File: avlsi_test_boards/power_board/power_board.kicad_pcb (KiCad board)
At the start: 4 copper layers, 100 x 100 mm, 100 parts, among them J1 PJ-102AH, J2 PJ-102AH, U1 TLV1117LV18DCYR, U11 TLV75709PDBV, U12 SN74LVC16T245DLR, U13 SN74LVC16T245DLR, U14 SN74LVC16T245DLR, U15 SN74LVC16T245DLR, U16 SN74LVC16T245DLR, U17 SN74LVC16T245DLR, U2 TLV1117LV25DCYR, U3 TLV1117LV33DCYR, U4 DS04-254-2-04BK-SMT, U5 74HC4051D_653, U6 TLV1117LV18DCYR, U7 TLV75709PDBV, U8 TLV1117LV25DCYR, U9 TLV1117LV33DCYR

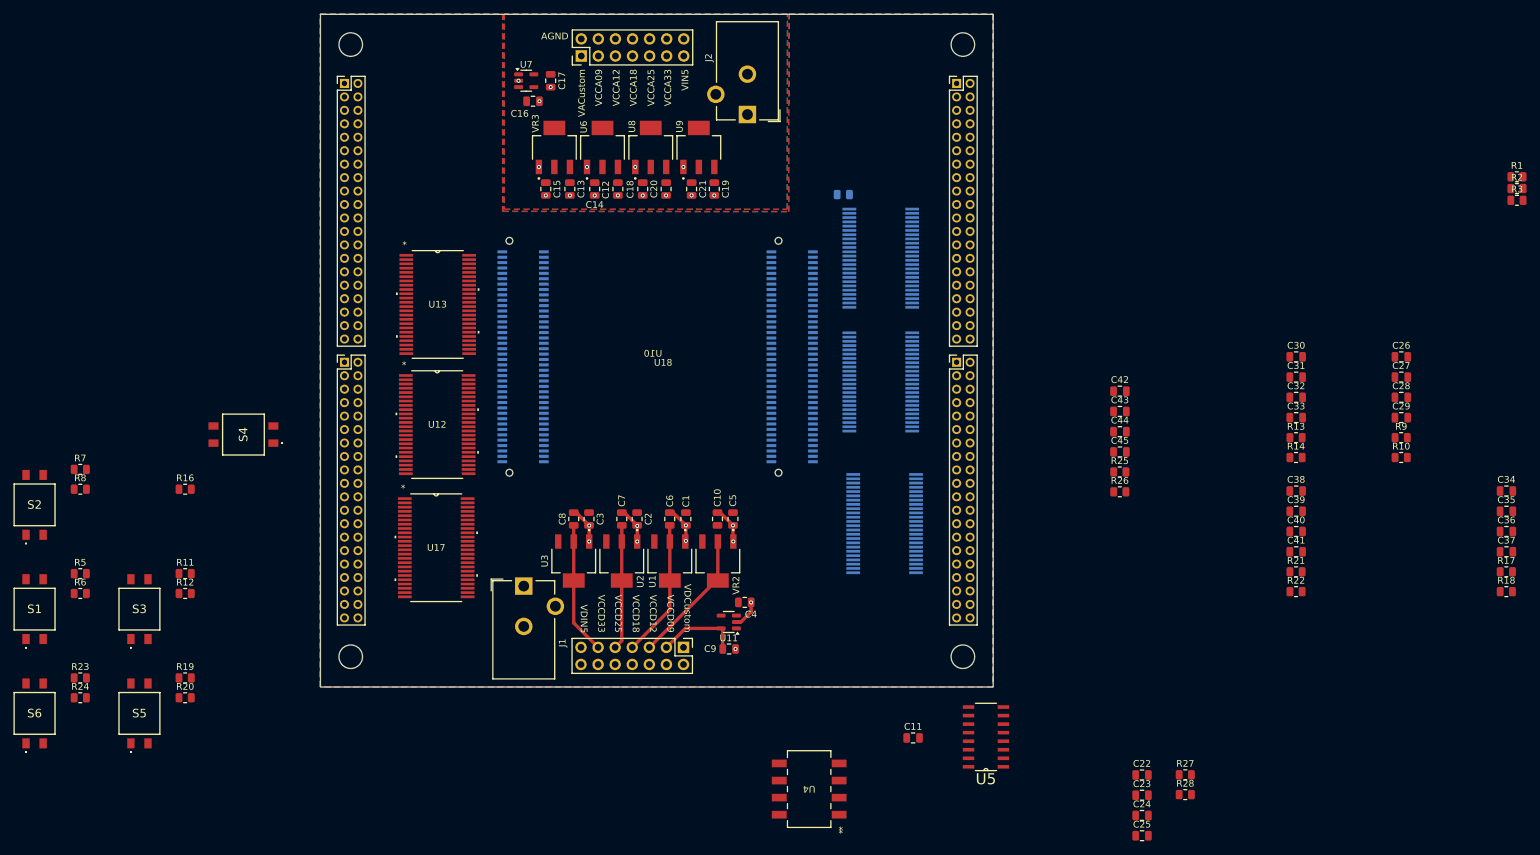
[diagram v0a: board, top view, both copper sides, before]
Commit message: Add 6 layer version of board
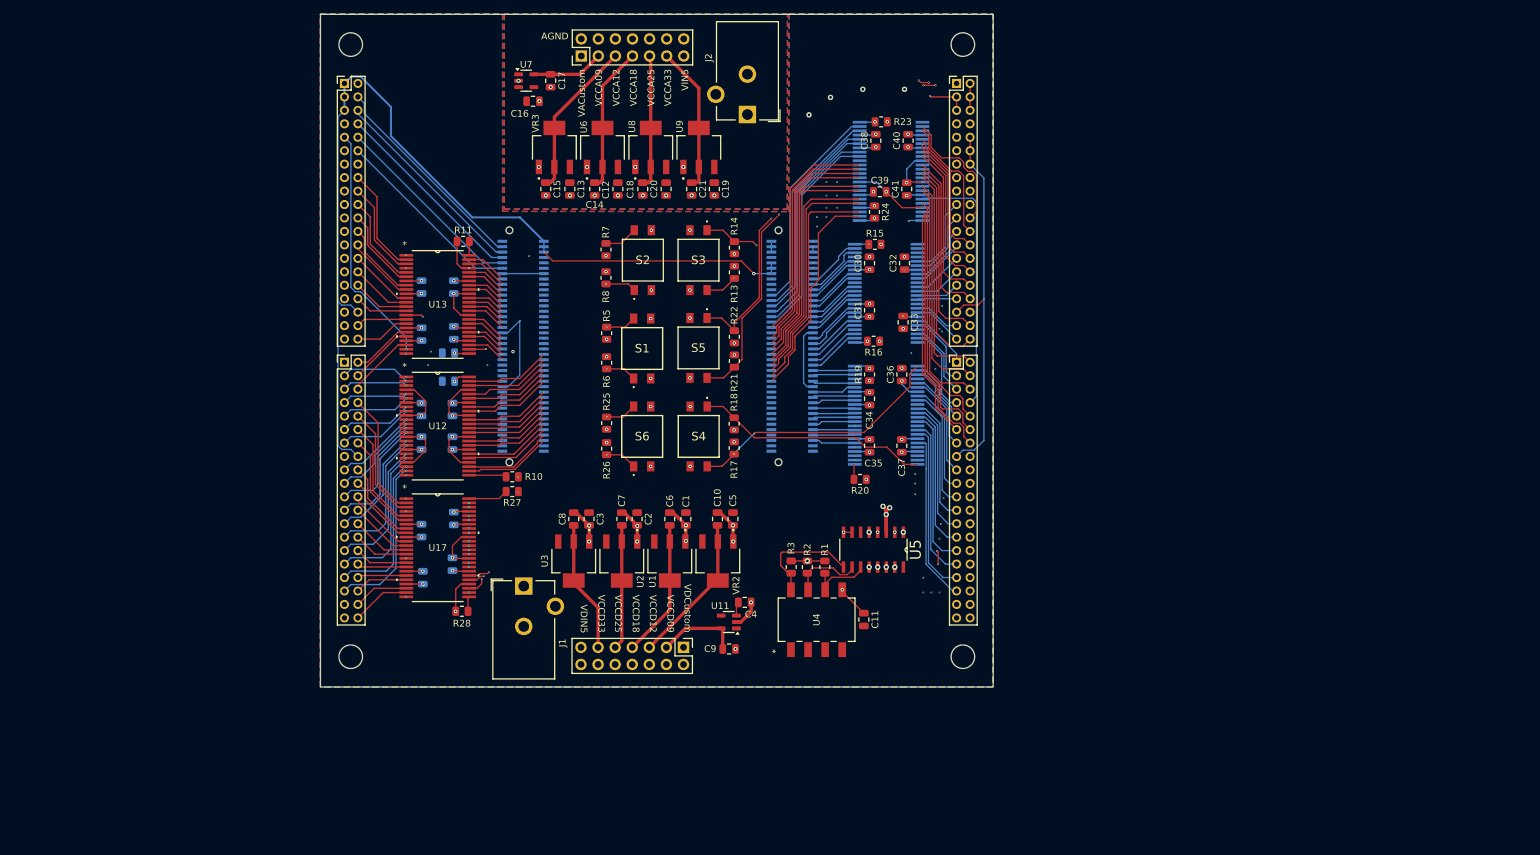
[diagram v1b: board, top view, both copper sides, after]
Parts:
- C22, C23, C24, C25, C26, C27, C28, C29, C42, C43, C44, C45, R12, R9: moved to B.Cu
- R15: moved to F.Cu
- moved C29 145.7 mm to (115.2, 89.2), turned to 90 degrees
- moved C28 145.7 mm to (115.2, 84.2), turned to -90 degrees
- moved R23 144.9 mm to (183.5, 41.4), turned to 180 degrees
- moved R9 141.9 mm to (119.2, 80.0)
- moved C27 141.4 mm to (119.8, 89.2), turned to 90 degrees
- moved C26 141.3 mm to (119.8, 84.2), turned to -90 degrees
- moved R24 138.4 mm to (182.5, 54.8), turned to -90 degrees
- moved C25 134.6 mm to (115.2, 66.0), turned to -90 degrees
- moved R10 132.2 mm to (128.7, 94.2), turned to 180 degrees
- moved C24 128.8 mm to (115.2, 73.0), turned to -90 degrees
- moved C22 125.4 mm to (120.0, 66.0), turned to -90 degrees
- moved C23 123.3 mm to (120.0, 72.8), turned to -90 degrees
- moved R3 120.9 mm to (170.2, 107.6), turned to -90 degrees
- moved R2 119.6 mm to (172.6, 107.6), turned to -90 degrees
- moved R1 118.1 mm to (175.2, 107.6), turned to -90 degrees
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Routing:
- net FPGA_33VDD: track 0.00 -> 272.7 mm, vias 0 -> 7
- net DGND: track 26.3 -> 155.3 mm, vias 10 -> 121
- net VCCD33: track 19.6 -> 100.2 mm, vias 0 -> 25
- net XADC_VP: track 0.00 -> 60.0 mm, vias 0 -> 1
- net FPGA_18VDD: track 0.00 -> 57.8 mm, vias 0 -> 1
- net XADC_VN: track 0.00 -> 57.6 mm, vias 0 -> 3
- net FPGA_VCDIN: track 0.00 -> 57.4 mm, vias 0 -> 1
- net /level_shifter5/DIR1: track 0.00 -> 57.1 mm, vias 0 -> 2
- net SYS_CLK_MC1: track 0.00 -> 54.2 mm, vias 0 -> 3
- net /level_shifter1/DIR2: track 0.00 -> 47.4 mm, vias 0 -> 2
- net /level_shifter5/DIR2: track 0.00 -> 47.1 mm, vias 0 -> 2
- net FPGA_TDO: track 0.00 -> 46.7 mm, vias 0 -> 1
- net MC1_79: track 0.00 -> 45.8 mm, vias 0 -> 1
- net VCCD18: track 20.5 -> 66.3 mm, vias 0 -> 1
- net MC1_77: track 0.00 -> 45.4 mm, vias 0 -> 1
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- added copper zone on In3.Cu, net DGND
- added copper zone on In4.Cu, net DGND
- added copper zone on In1.Cu, net VCCD33
- added copper zone on In2.Cu, net V_Level_Shift
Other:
- copper layers 4 -> 6

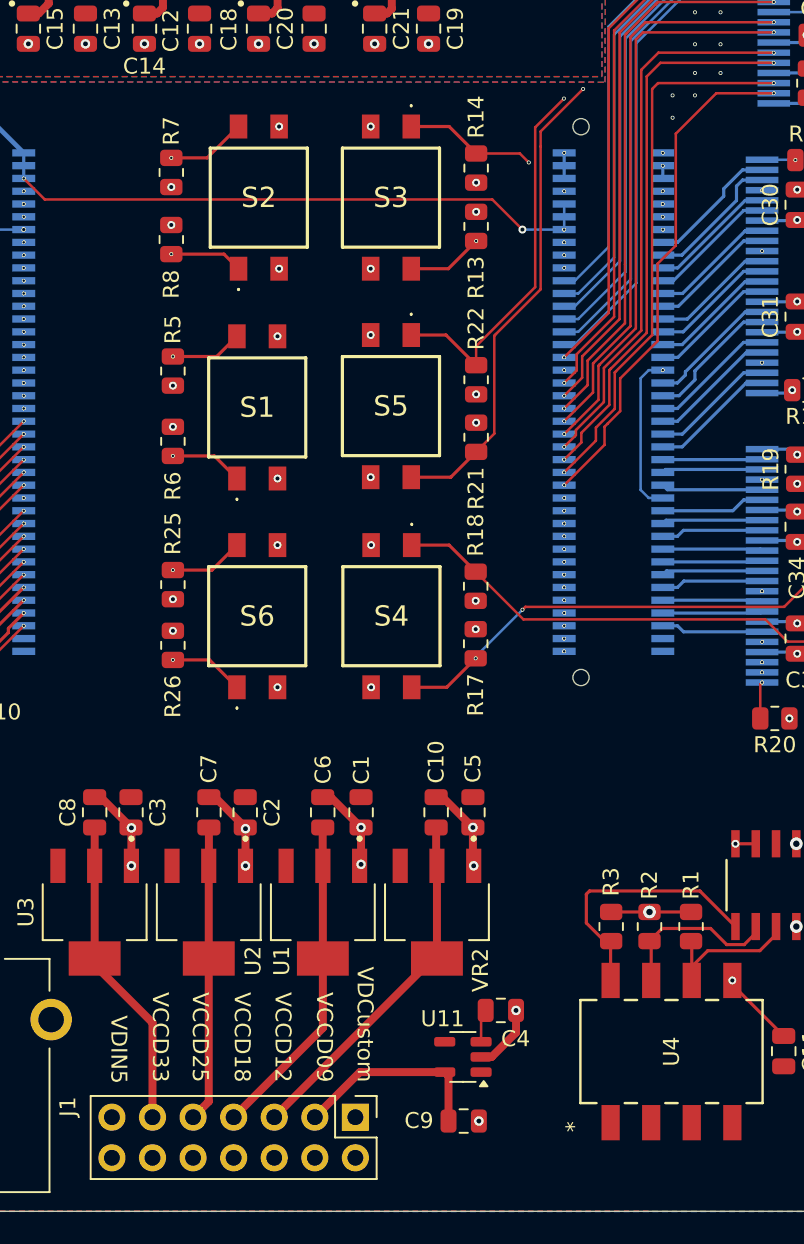
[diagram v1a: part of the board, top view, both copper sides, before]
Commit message: Add labels
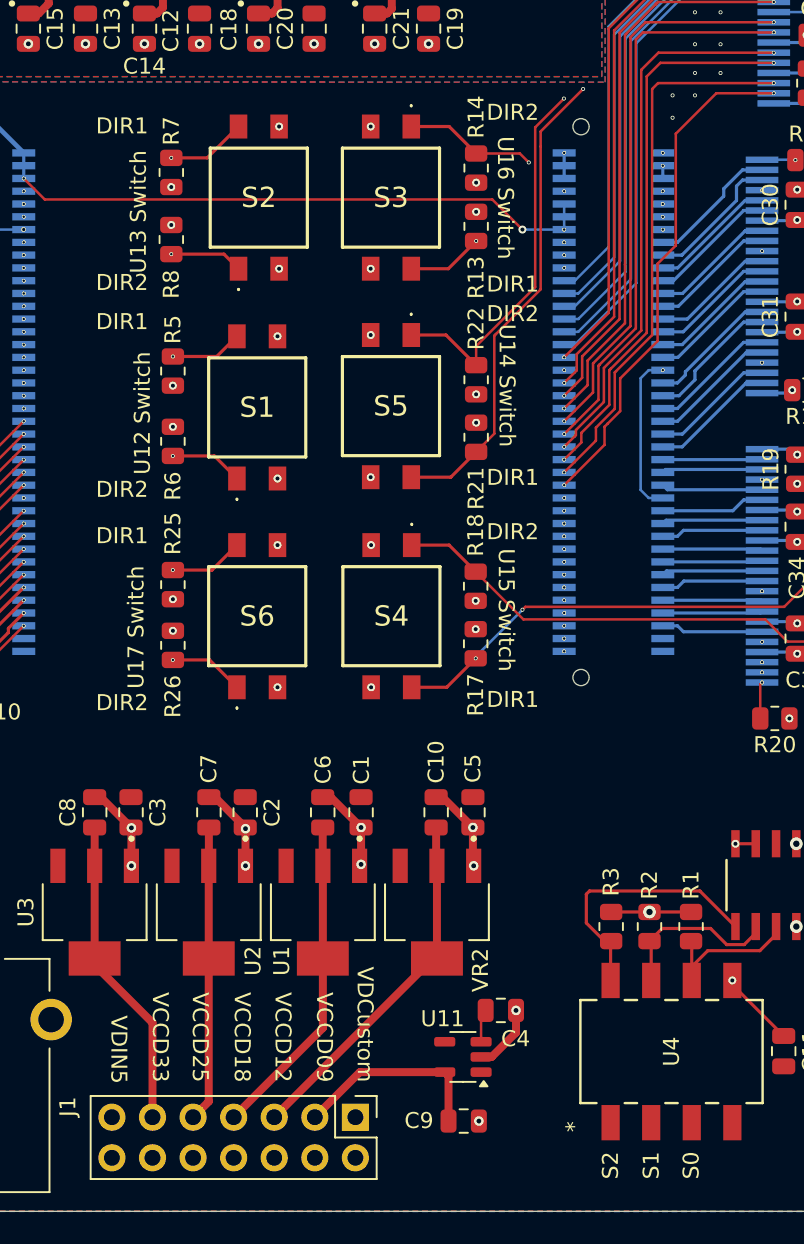
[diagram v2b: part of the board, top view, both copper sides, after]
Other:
- board text added: "DIR1"
- board text added: "DIR2"
- board text added: "S0"
- board text added: "S1"
- board text added: "S2"
- board text added: "U12 Switch"
- board text added: "U13 Switch"
- board text added: "U14 Switch"
- board text added: "U15 Switch"
- board text added: "U16 Switch"
- board text added: "U17 Switch"
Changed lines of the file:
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@@
+		)
+	)
+	(gr_text "DIR1"
+		(at 137.9 70.35 0)
+		(layer "F.SilkS")
+		(effects
+			(font
+				(size 1 1)
+				(thickness 0.15)
+			)
+			(justify left bottom)
 		)
 	)
@@
 		)
 	)
+	(gr_text "DIR1"
+		(at 137.9 83.75 0)
+		(layer "F.SilkS")
+		(effects
+			(font
+				(size 1 1)
+				(thickness 0.15)
+			)
+			(justify left bottom)
+		)
+	)
 	(gr_text "VCCD09"
 		(at 151.625 111.725 270)
@@
 		)
 	)
+	(gr_text "DIR2"
+		(at 162.35 69.85 0)
+		(layer "F.SilkS")
+		(effects
+			(font
+				(size 1 1)
+				(thickness 0.15)
+			)
+			(justify left bottom)
+		)
+	)
 	(gr_text "VCCD33"
 		(at 141.35 111.725 270)
@@
 		)
 	)
+	(gr_text "DIR2"
+		(at 137.9 67.9 0)
+		(layer "F.SilkS")
+		(effects
+			(font
+				(size 1 1)
+				(thickness 0.15)
+			)
+			(justify left bottom)
+		)
+	)
+	(gr_text "DIR2"
+		(at 137.9 94.2 0)
+		(layer "F.SilkS")
+		(effects
+			(font
+				(size 1 1)
+				(thickness 0.15)
+			)
+			(justify left bottom)
+		)
+	)
 	(gr_text "VCCD25"
 		(at 143.85 111.725 270)
@@
 		)
 	)
+	(gr_text "U12 Switch\n"
+		(at 141.4 79.35 90)
+		(layer "F.SilkS")
+		(effects
+			(font
+				(size 1 1)
+				(thickness 0.15)
+			)
+			(justify left bottom)
+		)
+	)
 	(gr_text "VIN5"
 		(at 154.975 36.825 90)
@@
 		)
 	)
+	(gr_text "DIR2"
+		(at 162.35 57.25 0)
+		(layer "F.SilkS")
+		(effects
+			(font
+				(size 1 1)
+				(thickness 0.15)
+			)
+			(justify left bottom)
+		)
+	)
 	(gr_text "VACustom"
 		(at 139.61 40.725 90)
@@
 		)
 	)
+	(gr_text "S1"
+		(at 173.25 123.45 90)
+		(layer "F.SilkS")
+		(effects
+			(font
+				(size 1 1)
+				(thickness 0.15)
+			)
+			(justify left bottom)
+		)
+	)
 	(gr_text "VCCA33"
 		(at 152.425 39.125 90)
@@
 		)
 	)
+	(gr_text "DIR1"
+		(at 162.35 94 0)
+		(layer "F.SilkS")
+		(effects
+			(font
+				(size 1 1)
+				(thickness 0.15)
+			)
+			(justify left bottom)
+		)
+	)
+	(gr_text "U16 Switch\n"
+		(at 162.95 58.15 270)
+		(layer "F.SilkS")
+		(effects
+			(font
+				(size 1 1)
+				(thickness 0.15)
+			)
+			(justify left bottom)
+		)
+	)
+	(gr_text "DIR2"
+		(at 162.35 83.5 0)
+		(layer "F.SilkS")
+		(effects
+			(font
+				(size 1 1)
+				(thickness 0.15)
+			)
+			(justify left bottom)
+		)
+	)
+	(gr_text "DIR1"
+		(at 162.35 80.1 0)
+		(layer "F.SilkS")
+		(effects
+			(font
+				(size 1 1)
+				(thickness 0.15)
+			)
+			(justify left bottom)
+		)
+	)
 	(gr_text "VDIN5"
 		(at 138.75 113.175 270)
@@
 		)
 	)
+	(gr_text "S0"
+		(at 175.75 123.45 90)
+		(layer "F.SilkS")
+		(effects
+			(font
+				(size 1 1)
+				(thickness 0.15)
+			)
+			(justify left bottom)
+		)
+	)
+	(gr_text "U13 Switch"
+		(at 141.15 66.75 90)
+		(layer "F.SilkS")
+		(effects
+			(font
+				(size 1 1)
+				(thickness 0.15)
+			)
+			(justify left bottom)
+		)
+	)
+	(gr_text "U14 Switch\n"
+		(at 163.05 69.9 270)
+		(layer "F.SilkS")
+		(effects
+			(font
+				(size 1 1)
+				(thickness 0.15)
+			)
+			(justify left bottom)
+		)
+	)
 	(gr_text "VCCA18"
 		(at 147.3 39.125 90)
 		(layer "F.SilkS")
 		(effects
+			(font
+				(size 1 1)
+				(thickness 0.15)
+			)
+			(justify left bottom)
+		)
+	)
+	(gr_text "U17 Switch\n"
+		(at 141 92.75 90)
+		(layer "F.SilkS")
+		(effects
+			(font
+				(size 1 1)
+				(thickness 0.15)
+			)
+			(justify left bottom)
+		)
+	)
+	(gr_text "DIR1"
+		(at 137.9 58.1 0)
+		(layer "F.SilkS")
+		(effects
+			(font
+				(size 1 1)
+				(thickness 0.15)
+			)
+			(justify left bottom)
+		)
+	)
+	(gr_text "S2"
+		(at 170.7 123.45 90)
+		(layer "F.SilkS")
+		(effects
+			(font
+				(size 1 1)
+				(thickness 0.15)
+			)
+			(justify left bottom)
+		)
+	)
+	(gr_text "DIR1"
+		(at 162.35 68 0)
+		(layer "F.SilkS")
+		(effects
+			(font
+				(size 1 1)
+				(thickness 0.15)
+			)
+			(justify left bottom)
+		)
+	)
+	(gr_text "DIR2"
+		(at 137.9 80.85 0)
+		(layer "F.SilkS")
+		(effects
+			(font
+				(size 1 1)
+				(thickness 0.15)
+			)
+			(justify left bottom)
+		)
+	)
+	(gr_text "U15 Switch\n"
+		(at 163 83.95 270)
+		(layer "F.SilkS")
+		(effects

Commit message: Update schematic
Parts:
- U18: footprint avlsi_preferred_parts:avlsi_power_board_opal_kelly -> avlsi_preferred_parts:power_board
- moved U18 3.06 mm to (151.0, 74.7)
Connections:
- net ADGND renamed AGND
- U18 pad 177: VCCD09 -> (no net)
- U18 pad 178: DGND -> (no net)
- U18 pad 179: VCCD12 -> VCCD09
- U18 pad 181: VCCD18 -> VCCD12
- U18 pad 183: VCCD25 -> VCCD18
- U18 pad 185: VCCD33 -> VCCD25
- U18 pad 187: DVIN5 -> VCCD33
- U5 pad 6: DVIN5 -> DGND
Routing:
- net FPGA_33VDD: track 272.7 -> 220.9 mm, vias 7 -> 6
- net MC1_23_PIN: track 18.5 -> 70.4 mm, vias 1 -> 2
- net DGND: track 155.3 -> 156.5 mm
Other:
- board size 100 x 100 mm -> 99.9 x 100 mm
- board text added: "Power and Interface Testing Board for Opal Kelly XEM7310-A75 Revison 1 Thomas Jagielski"
